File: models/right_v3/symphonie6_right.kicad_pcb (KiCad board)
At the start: 2 copper layers, 144.4 x 101 mm, 31 parts, among them SW0_1 SW_Push, SW0_2 SW_Push, SW0_3 SW_Push, SW0_4 SW_Push, SW0_5 SW_Push, SW1_0 SW_Push, SW1_2 SW_Push, SW1_3 SW_Push, SW1_4 SW_Push, SW2_0 SW_Push, SW2_1 SW_Push, SW2_3 SW_Push, SW2_4 SW_Push, SW3_0 SW_Push, SW3_1 SW_Push, SW3_2 SW_Push, SW3_4 SW_Push, SW4_0 SW_Push, SW4_1 SW_Push, SW4_2 SW_Push, SW4_3 SW_Push, SW5_0 SW_Push, SW5_1 SW_Push, SW5_2 SW_Push, SW5_3 SW_Push, SW5_4 SW_Push, SW6_0 SW_Push, SW6_1 SW_Push, SW6_2 SW_Push, SW6_3 SW_Push, SW6_4 SW_Push

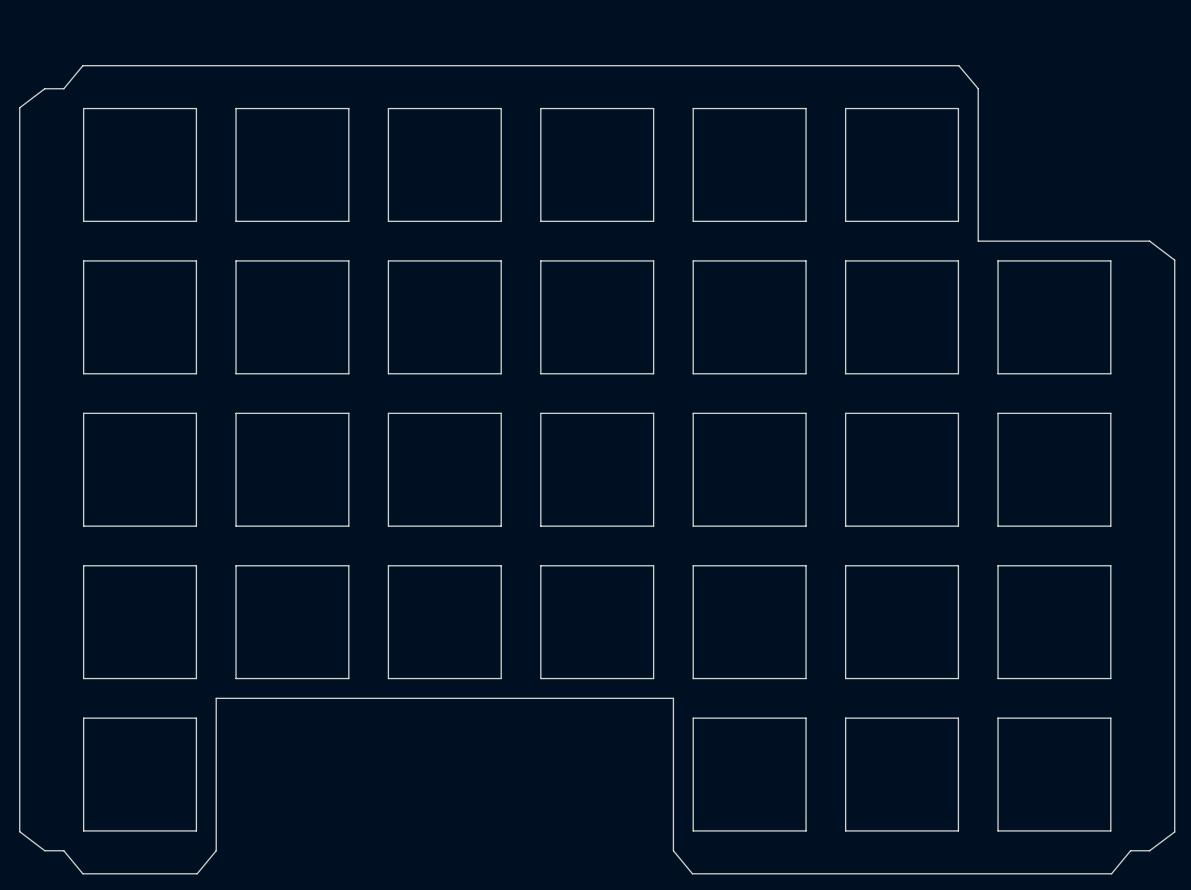
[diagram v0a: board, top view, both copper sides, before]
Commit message: feat: added several 3D models
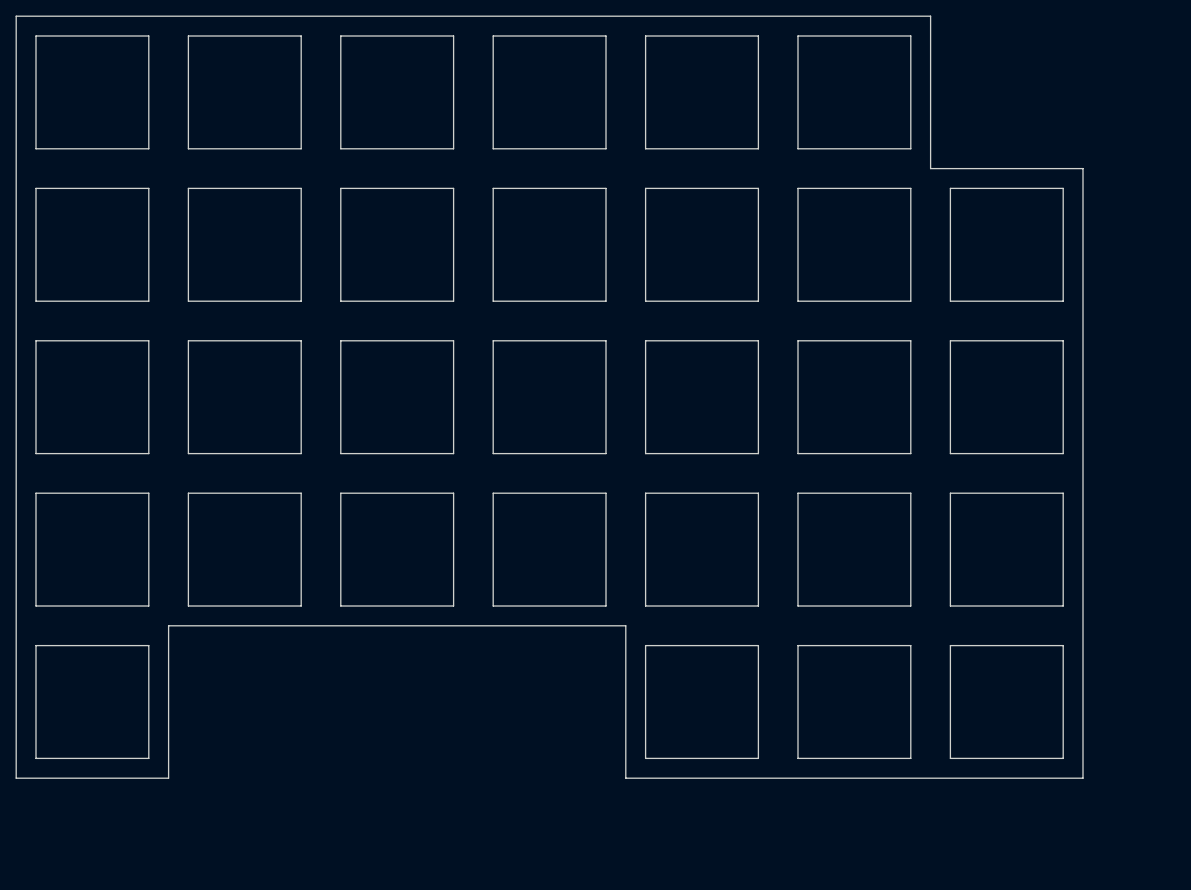
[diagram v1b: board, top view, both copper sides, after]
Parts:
- moved SW0_4 10.8 mm to (192.9, 90.5)
- moved SW0_5 10.8 mm to (231.0, 109.5)
- moved SW2_4 10.8 mm to (231.0, 90.5)
- moved SW4_3 10.8 mm to (135.7, 90.5)
- moved SW5_4 10.8 mm to (192.9, 109.5)
- moved SW2_0 10.8 mm to (135.7, 33.3)
- moved SW5_0 10.8 mm to (192.9, 33.3)
- moved SW0_2 10.8 mm to (231.0, 52.4)
- moved SW1_3 10.8 mm to (231.0, 71.4)
- moved SW2_1 10.8 mm to (135.7, 52.4)
- moved SW3_2 10.8 mm to (135.7, 71.4)
- moved SW5_1 10.8 mm to (192.9, 52.4)
- moved SW6_2 10.8 mm to (192.9, 71.4)
- moved SW1_4 10.8 mm to (211.9, 90.5)
- moved SW2_3 10.8 mm to (116.7, 90.5)
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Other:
- board size 144.4 x 101 mm -> 133.3 x 95.2 mm
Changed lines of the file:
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@@
 			(sketchpadsonfab no)
 			(subtractmaskfromsilk no)
-			(outputformat 1)
+			(outputformat 3)
 			(mirror no)
 			(drillshape 0)
 			(scaleselection 1)
-			(outputdirectory "../gerber/v0.0.2/symphonie6_right/")
+			(outputdirectory "./")
 		)
 	)
@@
 	(footprint "Salicylic-acid3-kbd_SW_Hole:SW_Hole_1u"
 		(layer "F.Cu")
-		(at 141.684425 99.55625)
+		(at 135.73125 90.4875)
 		(property "Reference" "SW4_3"
 			(at 7 8.1 0)
@@
 	(footprint "Salicylic-acid3-kbd_SW_Hole:SW_Hole_1u"
 		(layer "F.Cu")
-		(at 141.684425 80.50625)
+		(at 135.73125 71.4375)
 		(property "Reference" "SW3_2"
 			(at 7 8.1 0)
@@
 	(footprint "Salicylic-acid3-kbd_SW_Hole:SW_Hole_1u"
 		(layer "F.Cu")
-		(at 179.784425 99.55625)
+		(at 173.83125 90.4875)
 		(property "Reference" "SW6_3"
 			(at 7 8.1 0)
@@
 	(footprint "Salicylic-acid3-kbd_SW_Hole:SW_Hole_1u"
 		(layer "F.Cu")
-		(at 141.684425 42.40625)
+		(at 135.73125 33.3375)
 		(property "Reference" "SW2_0"
 			(at 7 8.1 0)
@@
 	(footprint "Salicylic-acid3-kbd_SW_Hole:SW_Hole_1u"
 		(layer "F.Cu")
-		(at 122.634425 61.45625)
+		(at 116.68125 52.3875)
 		(property "Reference" "SW0_1"
 			(at 7 8.1 0)
@@
 	(footprint "Salicylic-acid3-kbd_SW_Hole:SW_Hole_1u"
 		(layer "F.Cu")
-		(at 160.734425 80.50625)
+		(at 154.78125 71.4375)
 		(property "Reference" "SW4_2"
 			(at 7 8.1 0)
@@
 	(footprint "Salicylic-acid3-kbd_SW_Hole:SW_Hole_1u"
 		(layer "F.Cu")
-		(at 160.734425 99.55625)
+		(at 154.78125 90.4875)
 		(property "Reference" "SW5_3"
 			(at 7 8.1 0)
@@
 	(footprint "Salicylic-acid3-kbd_SW_Hole:SW_Hole_1u"
 		(layer "F.Cu")
-		(at 217.884425 61.45625)
+		(at 211.93125 52.3875)
 		(property "Reference" "SW6_1"
 			(at 7 8.1 0)
@@
 	(footprint "Salicylic-acid3-kbd_SW_Hole:SW_Hole_1u"
 		(layer "F.Cu")
-		(at 217.884425 80.50625)
+		(at 211.93125 71.4375)
 		(property "Reference" "SW0_3"
 			(at 7 8.1 0)
@@
 	(footprint "Salicylic-acid3-kbd_SW_Hole:SW_Hole_1u"
 		(layer "F.Cu")
-		(at 122.634425 99.55625)
+		(at 116.68125 90.4875)
 		(property "Reference" "SW2_3"
 			(at 7 8.1 0)
@@
 	(footprint "Salicylic-acid3-kbd_SW_Hole:SW_Hole_1u"
 		(layer "F.Cu")
-		(at 217.884425 42.40625)
+		(at 211.93125 33.3375)
 		(property "Reference" "SW6_0"
 			(at 7 8.1 0)
@@
 	(footprint "Salicylic-acid3-kbd_SW_Hole:SW_Hole_1u"
 		(layer "F.Cu")
-		(at 217.884425 99.55625)
+		(at 211.93125 90.4875)
 		(property "Reference" "SW1_4"
 			(at 7 8.1 0)
@@
 	(footprint "Salicylic-acid3-kbd_SW_Hole:SW_Hole_1u"
 		(layer "F.Cu")
-		(at 236.934425 80.50625)
+		(at 230.98125 71.4375)
 		(property "Reference" "SW1_3"
 			(at 7 8.1 0)
@@
 	(footprint "Salicylic-acid3-kbd_SW_Hole:SW_Hole_1u"
 		(layer "F.Cu")
-		(at 198.834425 99.55625)
+		(at 192.88125 90.4875)
 		(property "Reference" "SW0_4"
 			(at 7 8.1 0)
@@
 	(footprint "Salicylic-acid3-kbd_SW_Hole:SW_Hole_1u"
 		(layer "F.Cu")
-		(at 236.934425 61.45625)
+		(at 230.98125 52.3875)
 		(property "Reference" "SW0_2"
 			(at 7 8.1 0)
@@
 	(footprint "Salicylic-acid3-kbd_SW_Hole:SW_Hole_1u"
 		(layer "F.Cu")
-		(at 160.734425 42.40625)
+		(at 154.78125 33.3375)
 		(property "Reference" "SW3_0"
 			(at 7 8.1 0)
@@
 	(footprint "Salicylic-acid3-kbd_SW_Hole:SW_Hole_1u"
 		(layer "F.Cu")
-		(at 141.684425 61.45625)
+		(at 135.73125 52.3875)
 		(property "Reference" "SW2_1"
 			(at 7 8.1 0)
@@
 	(footprint "Salicylic-acid3-kbd_SW_Hole:SW_Hole_1u"
 		(layer "F.Cu")
-		(at 236.934425 118.60625)
+		(at 230.98125 109.5375)
 		(property "Reference" "SW0_5"
 			(at 7 8.1 0)
@@
 	(footprint "Salicylic-acid3-kbd_SW_Hole:SW_Hole_1u"
 		(layer "F.Cu")
-		(at 179.784425 42.40625)
+		(at 173.83125 33.3375)
 		(property "Reference" "SW4_0"
 			(at 7 8.1 0)
@@
 	(footprint "Salicylic-acid3-kbd_SW_Hole:SW_Hole_1u"
 		(layer "F.Cu")
-		(at 122.634425 42.40625)
+		(at 116.68125 33.3375)
 		(property "Reference" "SW1_0"
 			(at 7 8.1 0)
@@
 	(footprint "Salicylic-acid3-kbd_SW_Hole:SW_Hole_1u"
 		(layer "F.Cu")
-		(at 198.834425 42.40625)
+		(at 192.88125 33.3375)
 		(property "Reference" "SW5_0"
 			(at 7 8.1 0)
@@
 	(footprint "Salicylic-acid3-kbd_SW_Hole:SW_Hole_1u"
 		(layer "F.Cu")
-		(at 122.634425 118.60625)
+		(at 116.68125 109.5375)
 		(property "Reference" "SW3_4"
 			(at 7 8.1 0)
@@
 	(footprint "Salicylic-acid3-kbd_SW_Hole:SW_Hole_1u"
 		(layer "F.Cu")
-		(at 236.934425 99.55625)
+		(at 230.98125 90.4875)
 		(property "Reference" "SW2_4"
 			(at 7 8.1 0)
@@
 	(footprint "Salicylic-acid3-kbd_SW_Hole:SW_Hole_1u"
 		(layer "F.Cu")
-		(at 217.884425 118.60625)
+		(at 211.93125 109.5375)
 		(property "Reference" "SW6_4"
 			(at 7 8.1 0)
@@
 	(footprint "Salicylic-acid3-kbd_SW_Hole:SW_Hole_1u"
 		(layer "F.Cu")
-		(at 198.834425 61.45625)
+		(at 192.88125 52.3875)
 		(property "Reference" "SW5_1"
 			(at 7 8.1 0)
@@
 	(footprint "Salicylic-acid3-kbd_SW_Hole:SW_Hole_1u"
 		(layer "F.Cu")
-		(at 160.734425 61.45625)
+		(at 154.78125 52.3875)
 		(property "Reference" "SW3_1"
 			(at 7 8.1 0)
@@
 	(footprint "Salicylic-acid3-kbd_SW_Hole:SW_Hole_1u"
 		(layer "F.Cu")
-		(at 198.834425 118.60625)
+		(at 192.88125 109.5375)
 		(property "Reference" "SW5_4"
 			(at 7 8.1 0)
@@
 	(footprint "Salicylic-acid3-kbd_SW_Hole:SW_Hole_1u"
 		(layer "F.Cu")
-		(at 198.834425 80.50625)
+		(at 192.88125 71.4375)
 		(property "Reference" "SW6_2"
 			(at 7 8.1 0)
@@
 	(footprint "Salicylic-acid3-kbd_SW_Hole:SW_Hole_1u"
 		(layer "F.Cu")
-		(at 179.784425 61.45625)
+		(at 173.83125 52.3875)
 		(property "Reference" "SW4_1"
 			(at 7 8.1 0)
@@
 	(footprint "Salicylic-acid3-kbd_SW_Hole:SW_Hole_1u"
 		(layer "F.Cu")
-		(at 122.634425 80.50625)
+		(at 116.68125 71.4375)
 		(property "Reference" "SW1_2"
 			(at 7 8.1 0)
@@
 	(footprint "Salicylic-acid3-kbd_SW_Hole:SW_Hole_1u"
 		(layer "F.Cu")
-		(at 179.784425 80.50625)
+		(at 173.83125 71.4375)
 		(property "Reference" "SW5_2"
 			(at 7 8.1 0)
@@
 	)
 	(gr_line
-		(start 224.990625 30)
-		(end 227.409375 32.88125)
+		(start 107.15625 119.0625)
+		(end 107.15625 23.8125)
 		(stroke
 			(width 0.05)
@@
 	)
 	(gr_line
-		(start 115.490625 131.0125)
-		(end 129.778125 131.0125)
+		(start 183.35625 119.0625)
+		(end 183.35625 100.0125)
 		(stroke
 			(width 0.05)
@@
 	)
 	(gr_line
-		(start 251.971875 125.78125)
-		(end 251.971875 54.3125)
+		(start 221.45625 23.8125)
+		(end 221.45625 42.8625)
 		(stroke
 			(width 0.05)
@@
 	)
 	(gr_line
-		(start 227.409375 32.88125)
-		(end 227.409375 51.93125)
+		(start 126.20625 100.0125)
+		(end 126.20625 119.0625)
 		(stroke
 			(width 0.05)
@@
 	)
 	(gr_line
-		(start 110.728125 32.88125)
-		(end 107.596875 35.2625)
+		(start 126.20625 119.0625)
+		(end 107.15625 119.0625)
 		(stroke
 			(width 0.05)
@@
 	)
 	(gr_line
-		(start 189.309375 109.08125)
-		(end 189.309375 128.13125)
+		(start 107.15625 23.8125)
+		(end 221.45625 23.8125)
 		(stroke
 			(width 0.05)
@@
 	)
 	(gr_line
-		(start 113.109375 32.88125)
-		(end 115.490625 30)
+		(start 183.35625 100.0125)
+		(end 126.20625 100.0125)
 		(stroke
 			(width 0.05)
@@
 	)
 	(gr_line
-		(start 227.409375 51.93125)
-		(end 248.840625 51.93125)
+		(start 240.50625 42.8625)
+		(end 240.50625 119.0625)
 		(stroke
 			(width 0.05)
@@
 	)
 	(gr_line
-		(start 110.728125 128.13125)
-		(end 113.109375 128.13125)
+		(start 221.45625 42.8625)
+		(end 240.50625 42.8625)
 		(stroke
 			(width 0.05)
@@
 	)
 	(gr_line
-		(start 248.840625 51.93125)
-		(end 251.971875 54.3125)
-		(stroke
-			(width 0.05)
-			(type default)
-		)
-		(layer "Edge.Cuts")
-	)
-	(gr_line
-		(start 129.778125 131.0125)
-		(end 132.159375 128.13125)
-		(stroke
-			(width 0.05)
-			(type default)
-		)
-		(layer "Edge.Cuts")
-	)
-	(gr_line
-		(start 248.840625 128.13125)
-		(end 246.459375 128.13125)
-		(stroke
-			(width 0.05)
-			(type default)
-		)
-		(layer "Edge.Cuts")
-	)
-	(gr_line
-		(start 244.078125 131.0125)
-		(end 246.459375 128.13125)
-		(stroke
-			(width 0.05)
-			(type default)
-		)
-		(layer "Edge.Cuts")
-	)
-	(gr_line
-		(start 107.596875 125.75)
-		(end 110.728125 128.13125)
-		(stroke
-			(width 0.05)
-			(type default)
-		)
-		(layer "Edge.Cuts")
-	)
-	(gr_line
-		(start 191.690625 131.0125)
-		(end 189.309375 128.13125)
-		(stroke
-			(width 0.05)
-			(type default)
-		)
-		(layer "Edge.Cuts")
-	)
-	(gr_line
-		(start 113.109375 128.13125)
-		(end 115.490625 131.0125)
-		(stroke
-			(width 0.05)
-			(type default)
-		)
-		(layer "Edge.Cuts")
-	)
-	(gr_line
-		(start 132.159375 128.13125)
-		(end 132.159375 109.08125)
-		(stroke
-			(width 0.05)
-			(type default)
-		)
-		(layer "Edge.Cuts")
-	)
-	(gr_line
-		(start 191.690625 131.0125)
-		(end 244.078125 131.0125)
-		(stroke
-			(width 0.05)
-			(type default)
-		)
-		(layer "Edge.Cuts")
-	)
-	(gr_line
-		(start 113.109375 32.88125)
-		(end 110.728125 32.88125)
-		(stroke
-			(width 0.05)
-			(type default)
-		)
-		(layer "Edge.Cuts")
-	)
-	(gr_line
-		(start 107.596875 35.2625)
-		(end 107.596875 125.75)
-		(stroke
-			(width 0.05)
-			(type default)
-		)
-		(layer "Edge.Cuts")
-	)
-	(gr_line
-		(start 132.159375 109.08125)
-		(end 189.309375 109.08125)
-		(stroke
-			(width 0.05)
-			(type default)
-		)
-		(layer "Edge.Cuts")
-	)
-	(gr_line
-		(start 251.971875 125.78125)
-		(end 248.840625 128.13125)
-		(stroke
-			(width 0.05)
-			(type default)
-		)
-		(layer "Edge.Cuts")
-	)
-	(gr_line
-		(start 224.990625 30)
-		(end 115.490625 30)
+		(start 240.50625 119.0625)
+		(end 183.35625 119.0625)
 		(stroke
 			(width 0.05)
